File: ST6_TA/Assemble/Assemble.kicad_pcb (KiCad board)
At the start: 2 copper layers, 114.3 x 88.9 mm, 32 parts, among them SW1 SW_PUSH, SW10 SW_PUSH, SW11 SW_PUSH, SW2 SW_PUSH, SW3 SW_PUSH, SW4 SW_PUSH, SW5 SW_PUSH, SW6 SW_PUSH, SW7 SW_PUSH, SW8 SW_PUSH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

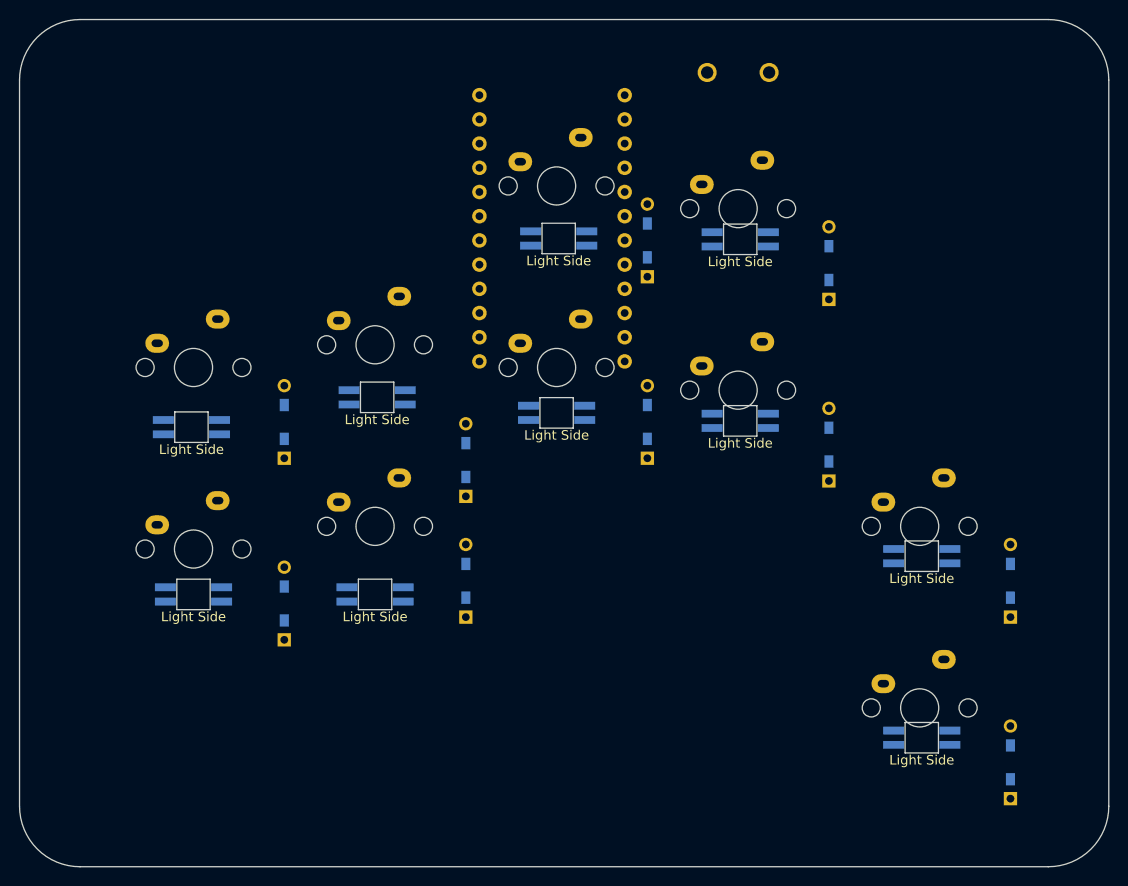
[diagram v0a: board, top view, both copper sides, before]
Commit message: ネジ穴検討
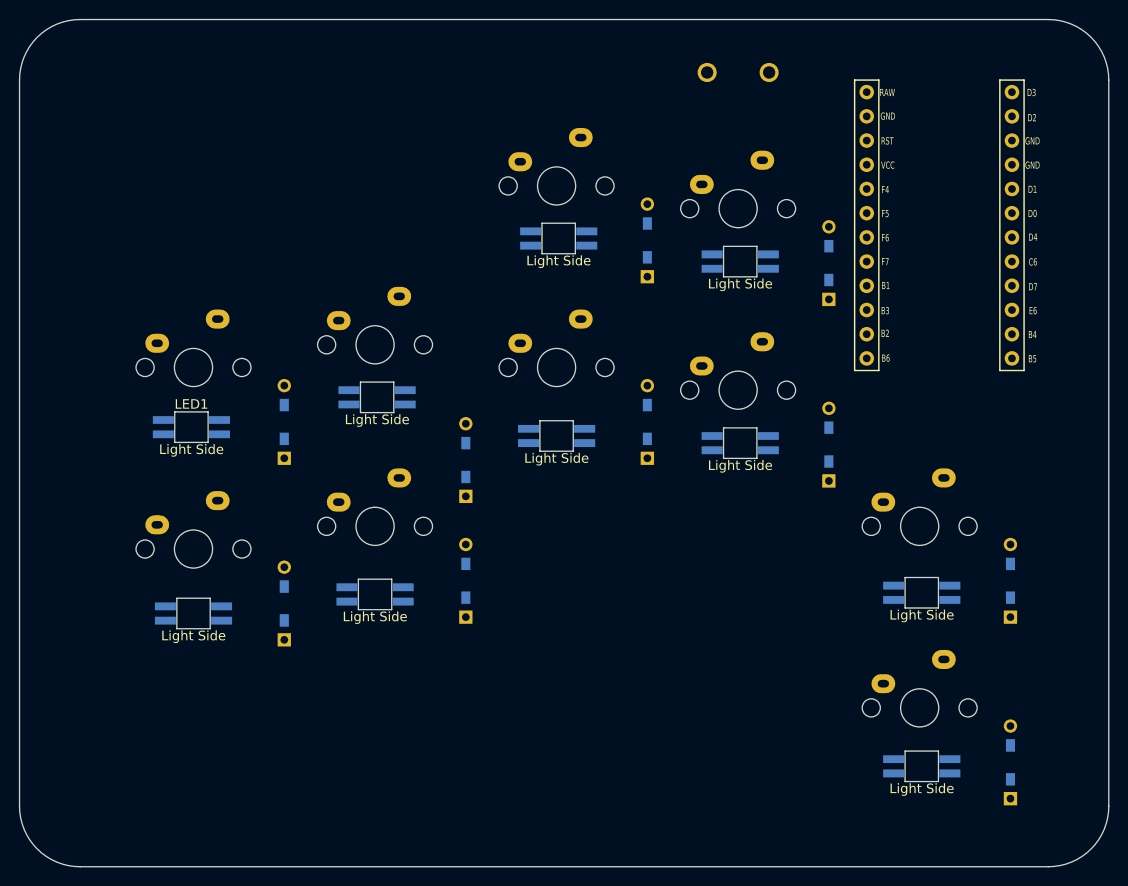
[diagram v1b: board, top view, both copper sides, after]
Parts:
- U1: moved to B.Cu
- moved U1 38.1 mm to (108.0, 122.4), turned to 180 degrees
- moved LED8 3.84 mm to (107.4, 161.8)
- moved LED7 3.00 mm to (107.4, 180.0)
- moved LED6 2.43 mm to (69.1, 145.3)
- moved LED10 2.34 mm to (88.3, 127.0)
- moved LED9 2.34 mm to (88.3, 146.1)
- moved LED2 2.00 mm to (31.0, 163.9)

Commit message: Top,Bottom,Assenbleのネジ穴確定
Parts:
- added Ref**: Val**, kbd_Hole:m2_Spacer_Hole_hex, F.Cu at (120.7, 108.0)
- added Ref**: Val**, kbd_Hole:m2_Spacer_Hole_hex, F.Cu at (19.1, 184.2)
- added Ref**: Val**, kbd_Hole:m2_Spacer_Hole_hex, F.Cu at (19.1, 108.0)
- added Ref**: Val**, kbd_Hole:m2_Spacer_Hole_hex, F.Cu at (120.7, 184.2)
- moved U1 1.60 mm to (107.0, 121.1)
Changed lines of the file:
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@@
     )
+  )
+  (footprint "kbd_Hole:m2_Spacer_Hole_hex" (layer "F.Cu")
+    (at 120.65 107.95)
+    (descr "Mounting Hole 2.2mm, no annular, M2")
+    (tags "mounting hole 2.2mm no annular m2")
+    (attr exclude_from_pos_files exclude_from_bom)
+    (fp_text reference "Ref**" (at 0 -3.2) (layer "F.Fab")
+        (effects (font (size 1 1) (thickness 0.15)))
+    )
+    (fp_text value "Val**" (at 0 3.2) (layer "F.Fab")
+        (effects (font (size 1 1) (thickness 0.15)))
+    )
+    (fp_line (start -2.4 0) (end -1.2 2.15)
+      (stroke (width 0.1) (type solid)) (layer "Edge.Cuts"))
+    (fp_line (start -1.2 -2.15) (end -2.4 0)
+      (stroke (width 0.1) (type solid)) (layer "Edge.Cuts"))
+    (fp_line (start -1.2 2.15) (end 1.2 2.15)
+      (stroke (width 0.1) (type solid)) (layer "Edge.Cuts"))
+    (fp_line (start 1.2 -2.15) (end -1.2 -2.15)
+      (stroke (width 0.1) (type solid)) (layer "Edge.Cuts"))
+    (fp_line (start 1.2 2.15) (end 2.4 0)
+      (stroke (width 0.1) (type solid)) (layer "Edge.Cuts"))
+    (fp_line (start 2.4 0) (end 1.2 -2.15)
+      (stroke (width 0.1) (type solid)) (layer "Edge.Cuts"))
   )
   (footprint "kbd_Parts:Diode_TH_SMD" (layer "F.Cu")
@@
       (net 5 "Net-(D3-A)") (pinfunction "2") (pintype "passive"))
   )
+  (footprint "kbd_Hole:m2_Spacer_Hole_hex" (layer "F.Cu")
+    (at 19.05 184.15)
+    (descr "Mounting Hole 2.2mm, no annular, M2")
+    (tags "mounting hole 2.2mm no annular m2")
+    (attr exclude_from_pos_files exclude_from_bom)
+    (fp_text reference "Ref**" (at 0 -3.2) (layer "F.Fab")
+        (effects (font (size 1 1) (thickness 0.15)))
+    )
+    (fp_text value "Val**" (at 0 3.2) (layer "F.Fab")
+        (effects (font (size 1 1) (thickness 0.15)))
+    )
+    (fp_line (start -2.4 0) (end -1.2 2.15)
+      (stroke (width 0.1) (type solid)) (layer "Edge.Cuts"))
+    (fp_line (start -1.2 -2.15) (end -2.4 0)
+      (stroke (width 0.1) (type solid)) (layer "Edge.Cuts"))
+    (fp_line (start -1.2 2.15) (end 1.2 2.15)
+      (stroke (width 0.1) (type solid)) (layer "Edge.Cuts"))
+    (fp_line (start 1.2 -2.15) (end -1.2 -2.15)
+      (stroke (width 0.1) (type solid)) (layer "Edge.Cuts"))
+    (fp_line (start 1.2 2.15) (end 2.4 0)
+      (stroke (width 0.1) (type solid)) (layer "Edge.Cuts"))
+    (fp_line (start 2.4 0) (end 1.2 -2.15)
+      (stroke (width 0.1) (type solid)) (layer "Edge.Cuts"))
+  )
   (footprint "kbd_SW:CherryMX_Solder_1u" (layer "F.Cu")
     (at 30.95625 157.1625)
@@
       (net 7 "Net-(D5-A)") (pinfunction "2") (pintype "passive"))
   )
+  (footprint "kbd_Hole:m2_Spacer_Hole_hex" (layer "F.Cu")
+    (at 19.05 107.95)
+    (descr "Mounting Hole 2.2mm, no annular, M2")
+    (tags "mounting hole 2.2mm no annular m2")
+    (attr exclude_from_pos_files exclude_from_bom)
+    (fp_text reference "Ref**" (at 0 -3.2) (layer "F.Fab")
+        (effects (font (size 1 1) (thickness 0.15)))
+    )
+    (fp_text value "Val**" (at 0 3.2) (layer "F.Fab")
+        (effects (font (size 1 1) (thickness 0.15)))
+    )
+    (fp_line (start -2.4 0) (end -1.2 2.15)
+      (stroke (width 0.1) (type solid)) (layer "Edge.Cuts"))
+    (fp_line (start -1.2 -2.15) (end -2.4 0)
+      (stroke (width 0.1) (type solid)) (layer "Edge.Cuts"))
+    (fp_line (start -1.2 2.15) (end 1.2 2.15)
+      (stroke (width 0.1) (type solid)) (layer "Edge.Cuts"))
+    (fp_line (start 1.2 -2.15) (end -1.2 -2.15)
+      (stroke (width 0.1) (type solid)) (layer "Edge.Cuts"))
+    (fp_line (start 1.2 2.15) (end 2.4 0)
+      (stroke (width 0.1) (type solid)) (layer "Edge.Cuts"))
+    (fp_line (start 2.4 0) (end 1.2 -2.15)
+      (stroke (width 0.1) (type solid)) (layer "Edge.Cuts"))
+  )
+  (footprint "kbd_Hole:m2_Spacer_Hole_hex" (layer "F.Cu")
+    (at 120.65 184.15)
+    (descr "Mounting Hole 2.2mm, no annular, M2")
+    (tags "mounting hole 2.2mm no annular m2")
+    (attr exclude_from_pos_files exclude_from_bom)
+    (fp_text reference "Ref**" (at 0 -3.2) (layer "F.Fab")
+        (effects (font (size 1 1) (thickness 0.15)))
+    )
+    (fp_text value "Val**" (at 0 3.2) (layer "F.Fab")
+        (effects (font (size 1 1) (thickness 0.15)))
+    )
+    (fp_line (start -2.4 0) (end -1.2 2.15)
+      (stroke (width 0.1) (type solid)) (layer "Edge.Cuts"))
+    (fp_line (start -1.2 -2.15) (end -2.4 0)
+      (stroke (width 0.1) (type solid)) (layer "Edge.Cuts"))
+    (fp_line (start -1.2 2.15) (end 1.2 2.15)
+      (stroke (width 0.1) (type solid)) (layer "Edge.Cuts"))
+    (fp_line (start 1.2 -2.15) (end -1.2 -2.15)
+      (stroke (width 0.1) (type solid)) (layer "Edge.Cuts"))
+    (fp_line (start 1.2 2.15) (end 2.4 0)
+      (stroke (width 0.1) (type solid)) (layer "Edge.Cuts"))
+    (fp_line (start 2.4 0) (end 1.2 -2.15)
+      (stroke (width 0.1) (type solid)) (layer "Edge.Cuts"))
+  )
   (footprint "kbd_Parts:Micon_ProMicro" (layer "B.Cu")
-    (at 107.95 122.428 180)
-    (property "Sheetfile" "Assemble.kicad_sch")
-    (property "Sheetname" "")
+    (at 107.01 121.138 180)
+    (property "Sheetfile" "Assemble.kicad_sch")
+    (property "Sheetname" "")

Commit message: 配線完了
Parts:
- removed Ref** (x4): Val**, kbd_Hole:m2_Spacer_Hole_hex
- moved U1 0.35 mm to (106.7, 121.2)
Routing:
- net VCC: track 0.00 -> 382.6 mm, vias 0 -> 10
- net GND: track 0.00 -> 303.8 mm
- net Low0: track 0.00 -> 228.5 mm, vias 0 -> 2
- net Low1: track 0.00 -> 202.1 mm
- net Col0: track 0.00 -> 136.4 mm
- net LED: track 0.00 -> 134.8 mm, vias 0 -> 2
- net Col1: track 0.00 -> 97.9 mm
- net Col2: track 0.00 -> 70.9 mm
- net Net-(LED6-DOUT): track 0.00 -> 53.7 mm
- net Net-(LED3-DOUT): track 0.00 -> 49.7 mm, vias 0 -> 5
- net Col4: track 0.00 -> 49.5 mm
- net Net-(LED4-DOUT): track 0.00 -> 48.2 mm, vias 0 -> 2
- net Net-(LED1-DOUT): track 0.00 -> 48.1 mm, vias 0 -> 4
- net Col3: track 0.00 -> 45.4 mm
- net Net-(LED5-DOUT): track 0.00 -> 43.9 mm, vias 0 -> 4
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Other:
- outline, holes or cut-outs redrawn

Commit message: ファイル名変更前
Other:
- board text added: "ST6_TA v1.0 PCB Design by @Coltvanilla"
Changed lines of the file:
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@@
     (pad_to_mask_clearance 0)
     (pcbplotparams
-      (layerselection 0x00010fc_ffffffff)
+      (layerselection 0x00010f0_ffffffff)
       (plot_on_all_layers_selection 0x0000000_00000000)
       (disableapertmacros false)
       (usegerberextensions false)
-      (usegerberattributes true)
-      (usegerberadvancedattributes true)
-      (creategerberjobfile true)
+      (usegerberattributes false)
+      (usegerberadvancedattributes false)
+      (creategerberjobfile false)
       (dashed_line_dash_ratio 12.000000)
       (dashed_line_gap_ratio 3.000000)
@@
       (outputformat 1)
       (mirror false)
-      (drillshape 1)
+      (drillshape 0)
       (scaleselection 1)
-      (outputdirectory "")
+      (outputdirectory "../発注/ST6_TA var1.0/")
     )
   )
@@
   (gr_line (start 21.45 184.15) (end 20.25 182)
     (stroke (width 0.1) (type default)) (layer "Edge.Cuts"))
+  (gr_text "ST6_TA v1.0 PCB Design by @Coltvanilla" (at 26.85 188.24) (layer "Edge.Cuts")
+    (effects (font (size 1 1) (thickness 0.15)) (justify left bottom))
+  )
   (segment (start 40.48125 140.0175) (end 33.49625 133.0325) (width 0.5) (layer "F.Cu") (net 1))
   (segment (start 40.48125 142.0525) (end 40.48125 140.0175) (width 0.5) (layer "B.Cu") (net 1))
